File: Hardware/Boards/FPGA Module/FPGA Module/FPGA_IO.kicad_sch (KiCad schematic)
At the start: 20 parts, among them U1 XCKU3P-FFVA676, U20 Si511J200

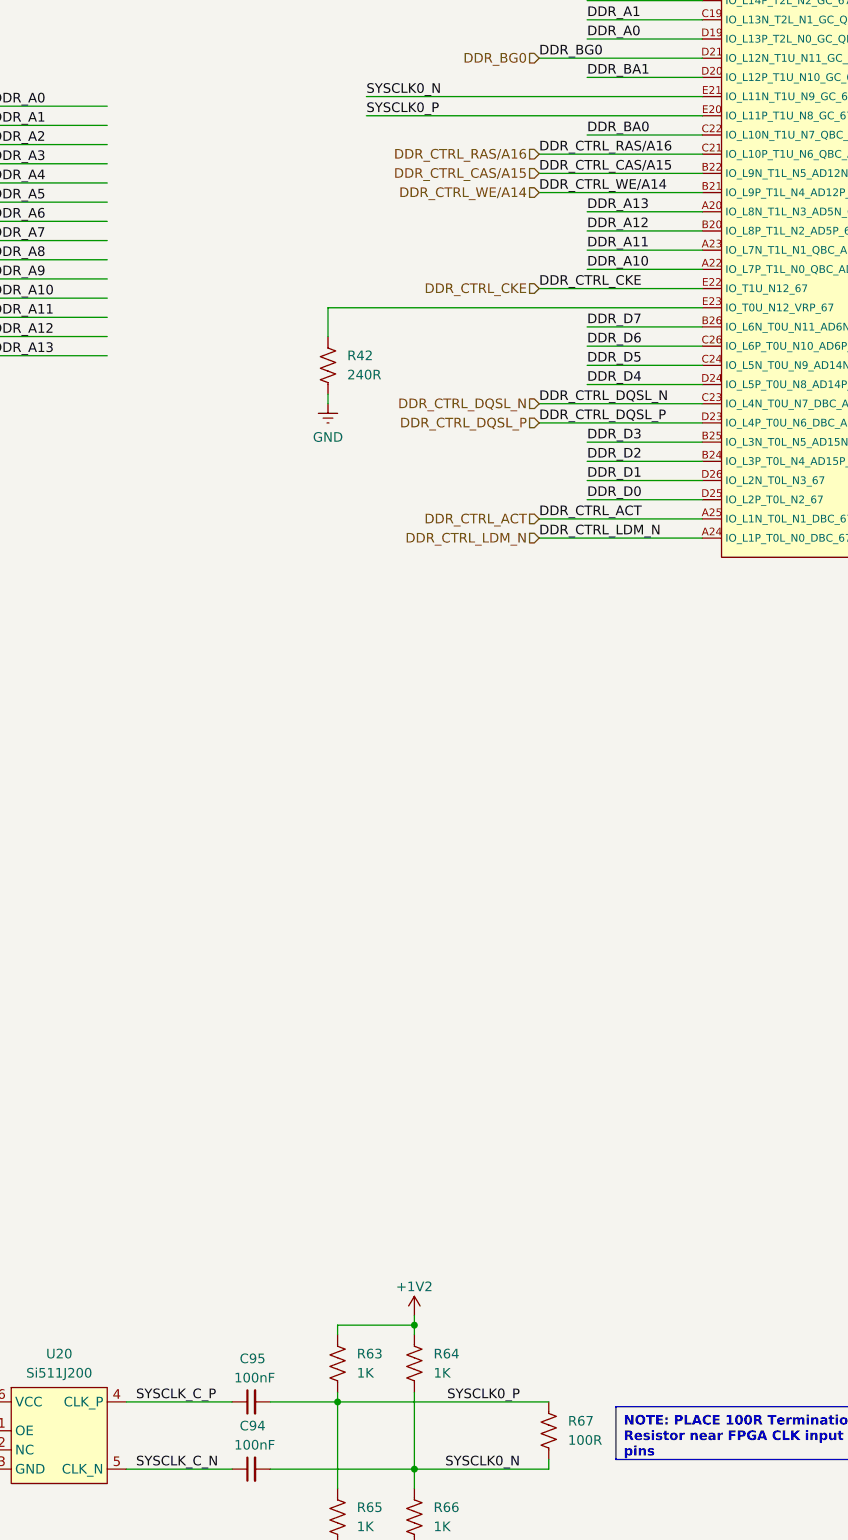
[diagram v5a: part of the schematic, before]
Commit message: Update FPGA Module Netclasses
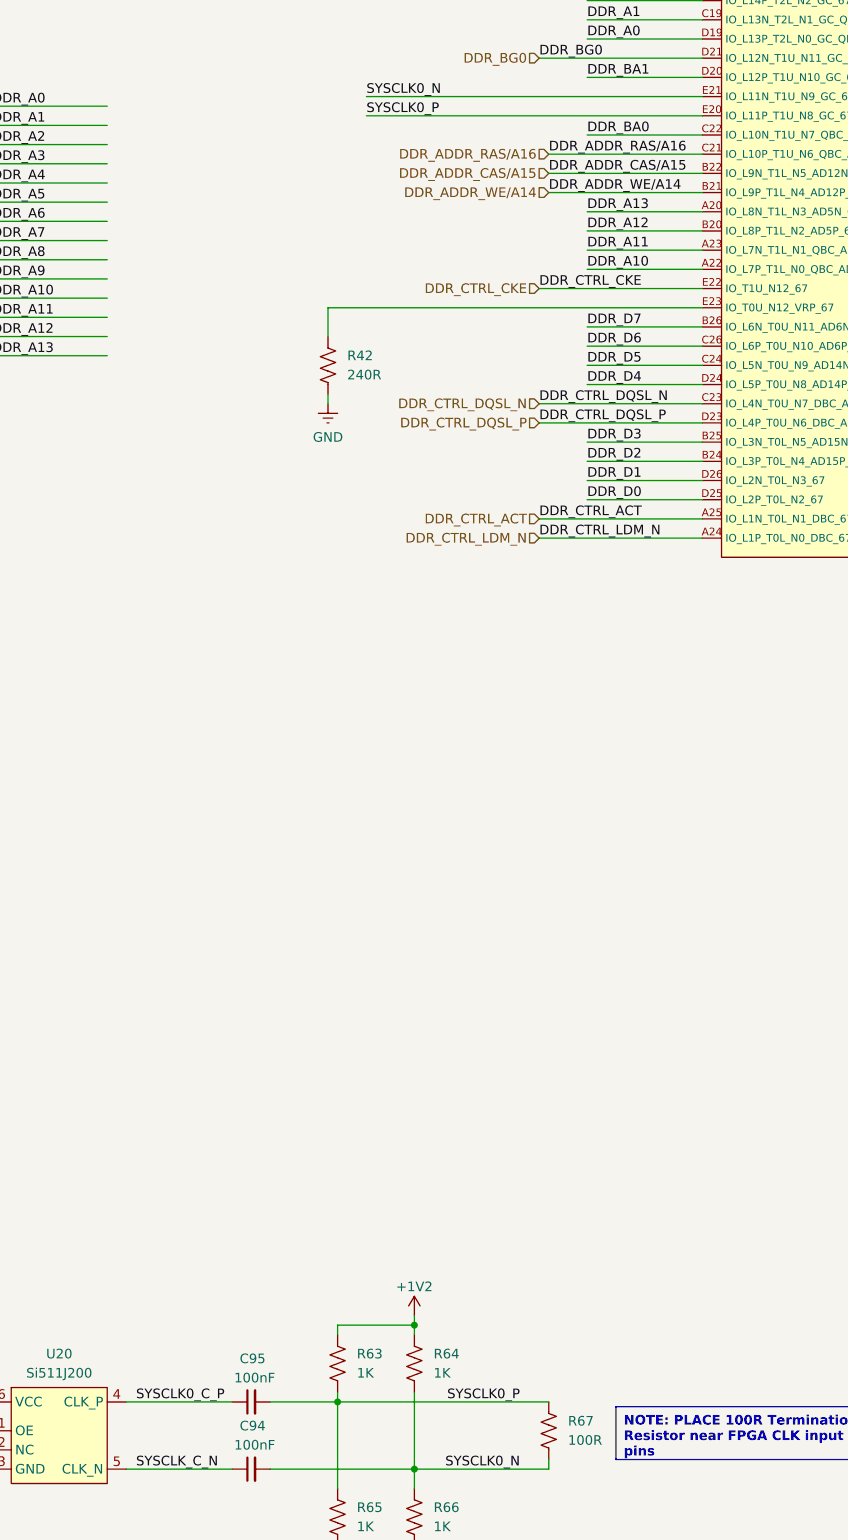
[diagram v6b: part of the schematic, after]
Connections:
- net DDR_CTRL_CAS/A15 renamed DDR_ADDR_CAS/A15
- net DDR_CTRL_RAS/A16 renamed DDR_ADDR_RAS/A16
- net DDR_CTRL_WE/A14 renamed DDR_ADDR_WE/A14
- net SYSCLK_C_P renamed SYSCLK0_C_P
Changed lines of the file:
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@@
 	(wire
 		(pts
-			(xy 129.54 116.84) (xy 151.13 116.84)
-		)
-		(stroke
-			(width 0)
-			(type default)
-		)
-	)
-	(wire
-		(pts
 			(xy 57.15 281.94) (xy 55.88 281.94)
 		)
@@
 	(wire
 		(pts
+			(xy 130.81 121.92) (xy 151.13 121.92)
+		)
+		(stroke
+			(width 0)
+			(type default)
+		)
+	)
+	(wire
+		(pts
 			(xy 304.8 265.43) (xy 287.02 265.43)
 		)
@@
 		)
 	)
+	(wire
+		(pts
+			(xy 130.81 119.38) (xy 151.13 119.38)
+		)
+		(stroke
+			(width 0)
+			(type default)
+		)
+	)
 	(bus
 		(pts
@@
 	(wire
 		(pts
-			(xy 129.54 119.38) (xy 151.13 119.38)
-		)
-		(stroke
-			(width 0)
-			(type default)
-		)
-	)
-	(wire
-		(pts
 			(xy 135.89 58.42) (xy 151.13 58.42)
 		)
@@
 		)
 	)
-	(wire
-		(pts
-			(xy 129.54 121.92) (xy 151.13 121.92)
-		)
-		(stroke
-			(width 0)
-			(type default)
-		)
-	)
 	(bus
 		(pts
@@
 	(wire
 		(pts
+			(xy 130.81 116.84) (xy 151.13 116.84)
+		)
+		(stroke
+			(width 0)
+			(type default)
+		)
+	)
+	(wire
+		(pts
 			(xy 261.62 307.34) (xy 285.75 307.34)
 		)
@@
 		)
 	)
-	(label "DDR_CTRL_CAS{slash}A15"
-		(at 129.54 119.38 0)
-		(fields_autoplaced yes)
-		(effects
-			(font
-				(size 1.27 1.27)
-			)
-			(justify left bottom)
-		)
-	)
 	(label "FIFO_D6"
 		(at 300.99 247.65 180)
@@
 		)
 	)
+	(label "DDR_ADDR_RAS{slash}A16"
+		(at 130.81 116.84 0)
+		(fields_autoplaced yes)
+		(effects
+			(font
+				(size 1.27 1.27)
+			)
+			(justify left bottom)
+		)
+	)
 	(label "DDR_D11"
 		(at 135.89 53.34 0)
@@
 		)
 	)
+	(label "DDR_ADDR_WE{slash}A14"
+		(at 130.81 121.92 0)
+		(fields_autoplaced yes)
+		(effects
+			(font
+				(size 1.27 1.27)
+			)
+			(justify left bottom)
+		)
+	)
 	(label "FIFO_D3"
 		(at 300.99 240.03 180)
@@
 		)
 	)
+	(label "DDR_ADDR_CAS{slash}A15"
+		(at 130.81 119.38 0)
+		(fields_autoplaced yes)
+		(effects
+			(font
+				(size 1.27 1.27)
+			)
+			(justify left bottom)
+		)
+	)
 	(label "MIPI_D1_P"
 		(at 510.54 347.98 0)
@@
 		)
 	)
-	(label "DDR_CTRL_WE{slash}A14"
-		(at 129.54 121.92 0)
-		(fields_autoplaced yes)
-		(effects
-			(font
-				(size 1.27 1.27)
-			)
-			(justify left bottom)
-		)
-	)
 	(label "HDMI_GTCLK_N"
 		(at 346.71 147.32 180)
@@
 		)
 	)
-	(label "SYSCLK_C_P"
+	(label "SYSCLK0_C_P"
 		(at 76.2 281.94 0)
 		(fields_autoplaced yes)
@@
 		)
 	)
-	(label "DDR_CTRL_RAS{slash}A16"
-		(at 129.54 116.84 0)
-		(fields_autoplaced yes)
-		(effects
-			(font
-				(size 1.27 1.27)
-			)
-			(justify left bottom)
-		)
-	)
 	(label "DDR_D6"
 		(at 57.15 46.99 0)
@@
 		)
 	)
+	(hierarchical_label "DDR_ADDR_RAS{slash}A16"
+		(shape input)
+		(at 130.81 116.84 180)
+		(fields_autoplaced yes)
+		(effects
+			(font
+				(size 1.27 1.27)
+			)
+			(justify right)
+		)
+	)
 	(hierarchical_label "MBUS_D[0..14]"
 		(shape input)
@@
 		)
 	)
-	(hierarchical_label "DDR_CTRL_RAS{slash}A16"
-		(shape input)
-		(at 129.54 116.84 180)
-		(fields_autoplaced yes)
-		(effects
-			(font
-				(size 1.27 1.27)
-			)
-			(justify right)
-		)
-	)
 	(hierarchical_label "FIFO_CLK"
 		(shape input)
@@
 		)
 	)
-	(hierarchical_label "DDR_CTRL_CAS{slash}A15"
+	(hierarchical_label "DDR_ADDR_CAS{slash}A15"
 		(shape input)
-		(at 129.54 119.38 180)
+		(at 130.81 119.38 180)
 		(fields_autoplaced yes)
 		(effects
@@
 		)
 	)
-	(hierarchical_label "DDR_CTRL_WE{slash}A14"
-		(shape input)
-		(at 129.54 121.92 180)
-		(fields_autoplaced yes)
-		(effects
-			(font
-				(size 1.27 1.27)
-			)
-			(justify right)
-		)
-	)
 	(hierarchical_label "UART_RX"
 		(shape input)
@@
 		(fields_autoplaced yes)
 		(effects
+			(font
+				(size 1.27 1.27)
+			)
+			(justify right)
+		)
+	)
+	(hierarchical_label "DDR_ADDR_WE{slash}A14"
+		(shape input)
+		(at 130.81 121.92 180)
+		(fields_autoplaced yes)
+		(effects

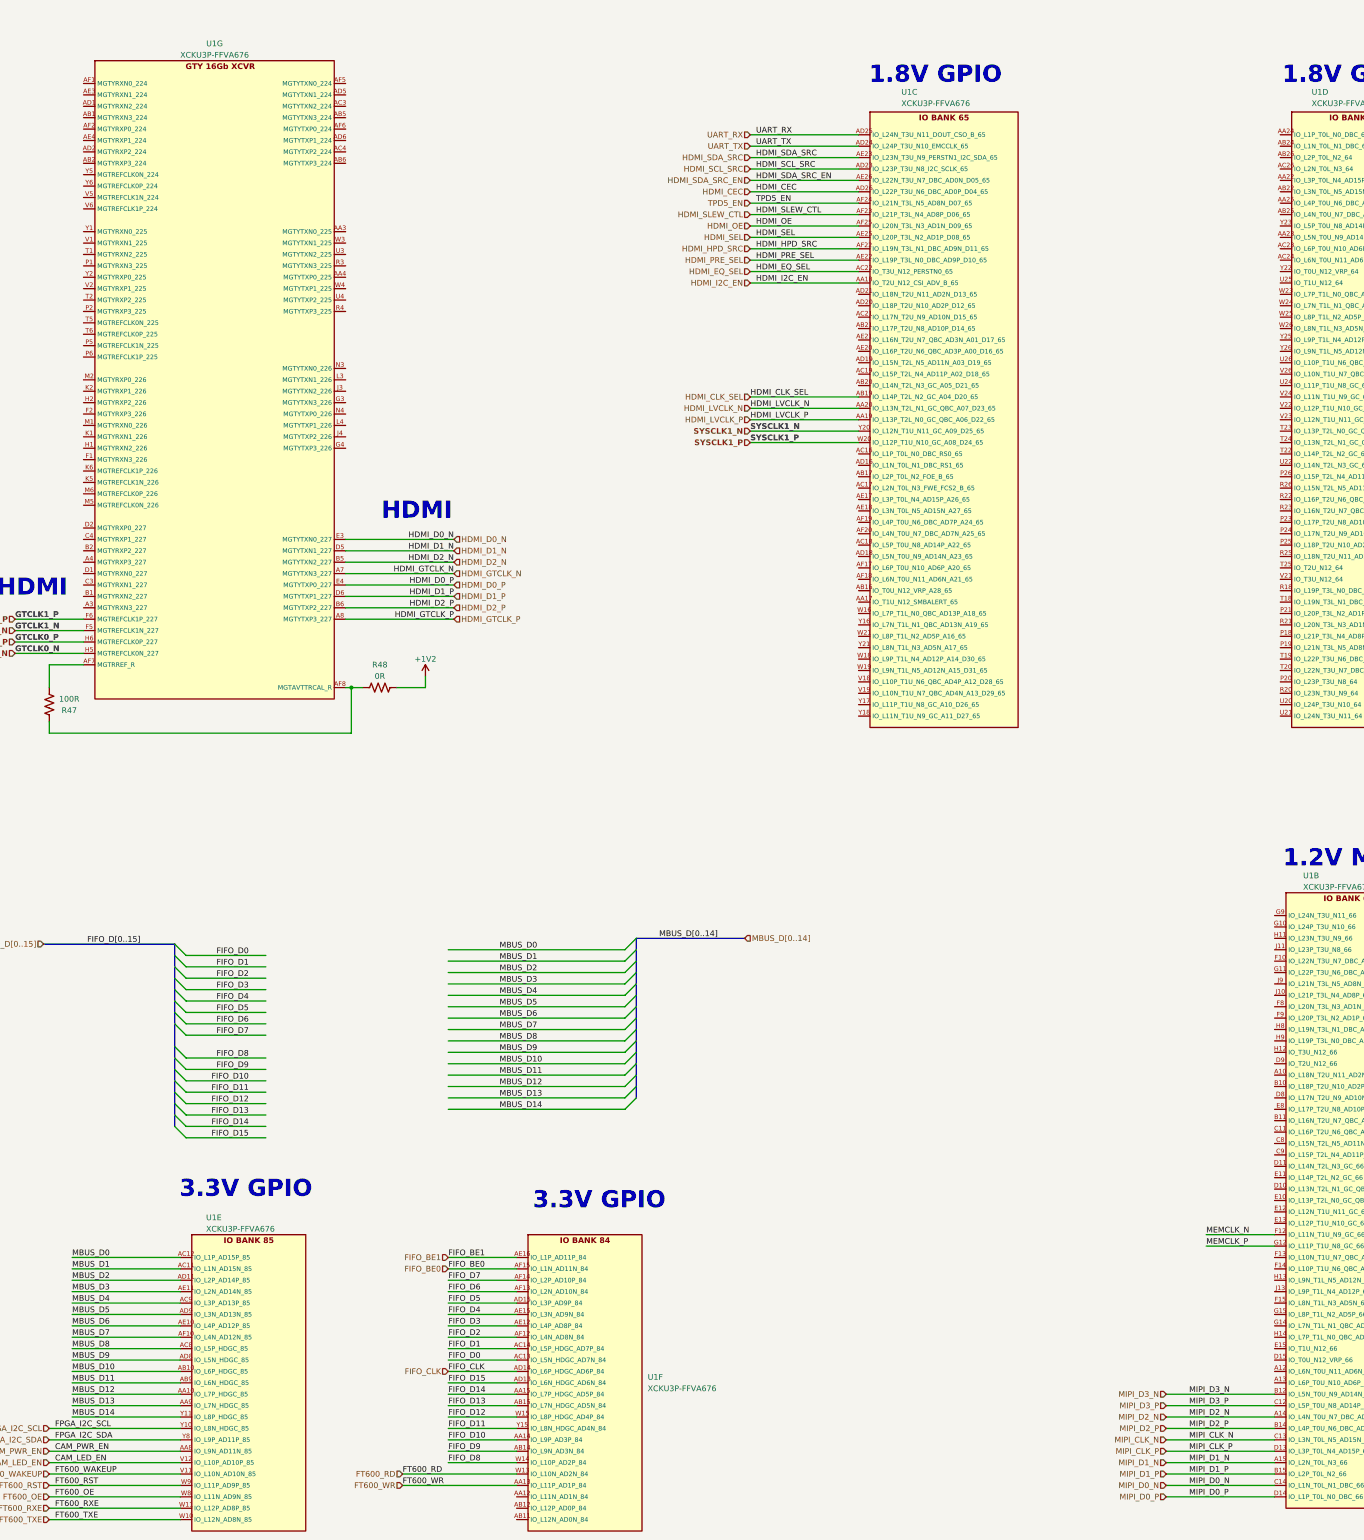
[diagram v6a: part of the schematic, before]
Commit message: Added NC to unused pins
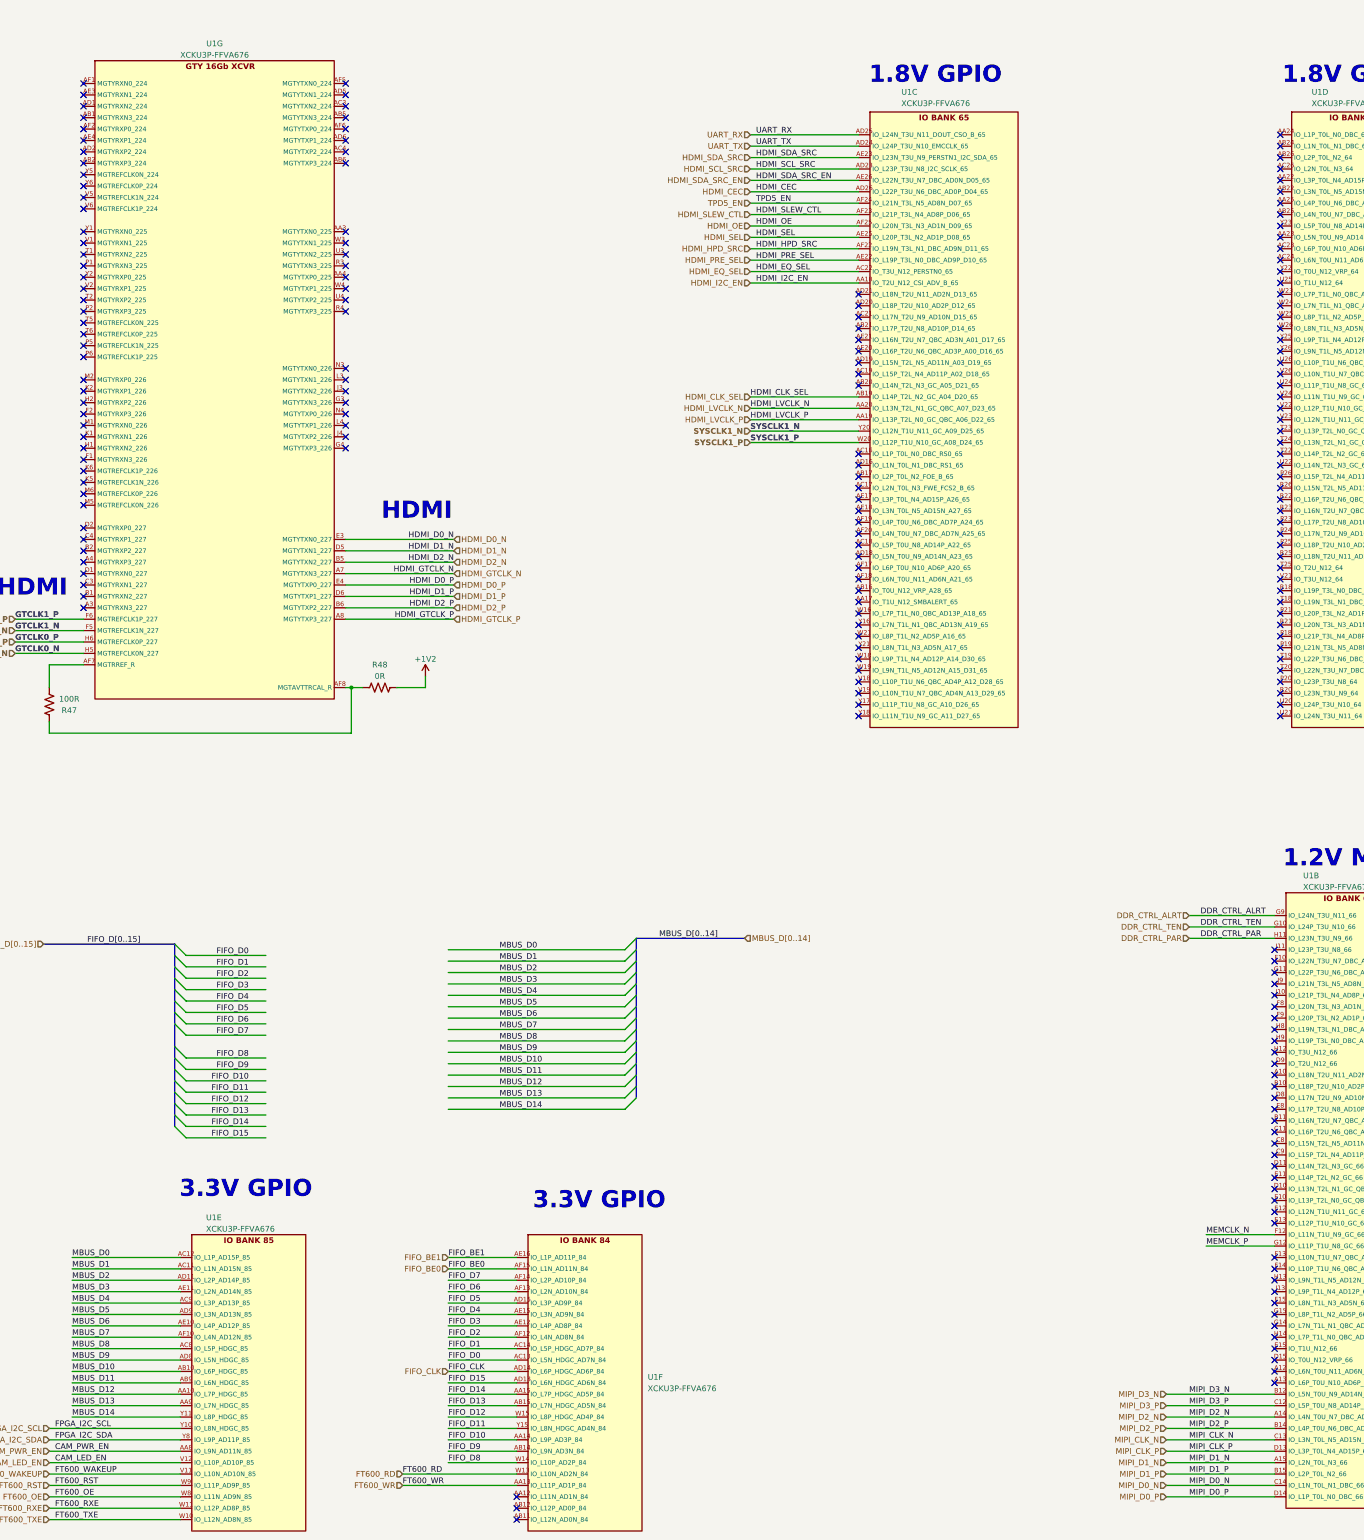
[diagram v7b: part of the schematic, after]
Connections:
- net DDR_CTRL_TEN: now reaches U1.G10 (IO_L24P_T3U_N10_66)
- net DDR_CTRL_ALRT: now reaches U1.G9 (IO_L24N_T3U_N11_66)
- net DDR_CTRL_PAR: now reaches U1.H11 (IO_L23N_T3U_N9_66)
- no-connect marks 1 -> 194

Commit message: FPGA Module sch update
Added 3V3 LDO for MCU and 3V3 EN for DCDC. Also added SPI bus from MCU to FPGA with level shifter
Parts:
- added C137, C138: 100nF, Capacitor_SMD:C_0201_0603Metric, symbol Device:C_Small
- added D12: LED3, LED_SMD:LED_0603_1608Metric, symbol Device:LED
- added D3: LED0, LED_SMD:LED_0603_1608Metric, symbol Device:LED
- added D5: LED1, LED_SMD:LED_0603_1608Metric, symbol Device:LED
- added D7: LED2, LED_SMD:LED_0603_1608Metric, symbol Device:LED
- added Q10, Q7, Q8, Q9: IRLML6244, Package_TO_SOT_SMD:SOT-23, symbol Transistor_FET:IRLML6244
- added R113, R114, R115, R116, R117, R118, R119, R120: 10K, Resistor_SMD:R_0402_1005Metric, symbol Device:R_US
- added R121, R122, R123, R124, R125, R126, R127, R128: 100R, Resistor_SMD:R_0402_1005Metric, symbol Device:R_US
- added TP10: IO7, FPGA Module:Test Point 0.75mm, symbol Connector:TestPoint
- added TP11, TP12, TP13, TP14, TP15, TP16: Test Point, FPGA Module:Test Point 0.75mm, symbol Connector:TestPoint
- added TP3: IO0, FPGA Module:Test Point 0.75mm, symbol Connector:TestPoint
- added TP4: IO1, FPGA Module:Test Point 0.75mm, symbol Connector:TestPoint
- added TP5: IO2, FPGA Module:Test Point 0.75mm, symbol Connector:TestPoint
- added TP6: IO3, FPGA Module:Test Point 0.75mm, symbol Connector:TestPoint
- added TP7: IO4, FPGA Module:Test Point 0.75mm, symbol Connector:TestPoint
- added TP8: IO5, FPGA Module:Test Point 0.75mm, symbol Connector:TestPoint
- added TP9: IO6, FPGA Module:Test Point 0.75mm, symbol Connector:TestPoint
- added U15: TXB0108DQSR, Package_SON:USON-20_2x4mm_P0.4mm, symbol Logic_LevelTranslator:TXB0108DQSR
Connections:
- net +1V8: now also C137.1, U15.16 (VCCB)
- net GND: now also C137.2, C138.2, Q10.2 (S), Q7.2 (S), Q8.2 (S), Q9.2 (S), R114.1, R116.1, R118.1, R120.1, U15.15 (GND)
- net MEMCLK_N: now also TP16.1
- net MEMCLK_P: now also TP15.1
- net SYSCLK0_C_P: now also TP11.1
- net SYSCLK0_N: now also TP14.1
- net SYSCLK0_P: now also TP13.1
- net IO5: now reaches U1.AA17 (IO_T1U_N12_SMBALERT_65)
- net IO5: now also R126.1
- net IO4: now reaches U1.AB16 (IO_T0U_N12_VRP_A28_65)
- net IO4: now also R125.1
- net IO0: now reaches U1.AC18 (IO_L5P_T0U_N8_AD14P_A22_65)
- net IO0: now also R121.1
- net IO1: now reaches U1.AD18 (IO_L5N_T0U_N9_AD14N_A23_65)
- net IO1: now also R122.1
- net IO2: now reaches U1.AF17 (IO_L6P_T0U_N10_AD6P_A20_65)
- net IO2: now also R123.1
- net IO3: now reaches U1.AF18 (IO_L6N_T0U_N11_AD6N_A21_65)
- net IO3: now also R124.1
- net FPGA_SPI_MISO: now reaches U1.V18 (IO_L10P_T1U_N6_QBC_AD4P_A12_D28_65)
- net FPGA_SPI_MISO: now also U15.20 (B1)
- net FPGA_SPI_CS: now reaches U1.V19 (IO_L10N_T1U_N7_QBC_AD4N_A13_D29_65)
- net FPGA_SPI_CS: now also U15.19 (B2)
- net IO6: now reaches U1.W16 (IO_L7P_T1L_N0_QBC_AD13P_A18_65)
- net IO6: now also R127.1
- net LED1: now reaches U1.W18 (IO_L9P_T1L_N4_AD12P_A14_D30_65)
- net LED1: now also Q8.1 (G), R116.2
- net LED0: now reaches U1.W19 (IO_L9N_T1L_N5_AD12N_A15_D31_65)
- net LED0: now also Q7.1 (G), R114.2
- net LED3: now reaches U1.W21 (IO_L8P_T1L_N2_AD5P_A16_65)
- net LED3: now also Q10.1 (G), R120.2
- net IO7: now reaches U1.Y16 (IO_L7N_T1L_N1_QBC_AD13N_A19_65)
- net IO7: now also R128.1
- net FPGA_SPI_SCK: now reaches U1.Y17 (IO_L11P_T1U_N8_GC_A10_D26_65)
- net FPGA_SPI_SCK: now also U15.18 (B3)
- net FPGA_SPI_MOSI: now reaches U1.Y18 (IO_L11N_T1U_N9_GC_A11_D27_65)
- net FPGA_SPI_MOSI: now also U15.17 (B4)
- net LED2: now reaches U1.Y21 (IO_L8N_T1L_N3_AD5N_A17_65)
- net LED2: now also Q9.1 (G), R118.2
- net SYSCLK_C_N renamed SYSCLK0_C_N
- net SYSCLK0_C_N: now also TP12.1
- new net: D12.1 (K), Q10.3 (D)
- new net: D7.1 (K), Q9.3 (D)
- new net: D7.2 (A), R117.1
- new net: D3.2 (A), R113.1
- new net: D5.2 (A), R115.1
- new net: D12.2 (A), R119.1
- new net: D5.1 (K), Q8.3 (D)
- new net: D3.1 (K), Q7.3 (D)
- new net +3V3: C138.1, R113.2, R115.2, R117.2, R119.2, U15.5 (VCCA)
- new net IO0_R: R121.2, TP3.1
- new net IO1_R: R122.2, TP4.1
- new net IO2_R: R123.2, TP5.1
- new net IO3_R: R124.2, TP6.1
- new net IO4_R: R125.2, TP7.1
- new net IO5_R: R126.2, TP8.1
- new net IO6_R: R127.2, TP9.1
- new net IO7_R: R128.2, TP10.1
- new net LVL_SHIFT_EN: U15.6 (OE)
- new net SYS_SPI_CS: U15.2 (A2)
- new net SYS_SPI_MISO: U15.1 (A1)
- new net SYS_SPI_MOSI: U15.4 (A4)
- new net SYS_SPI_SCK: U15.3 (A3)
- no-connect marks 194 -> 186
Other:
- moved on the sheet: C110, C111, C93, C94, C95, R63, R64, R65, R66, R67, R75, R76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
